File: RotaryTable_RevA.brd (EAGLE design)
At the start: 90 x 70 mm, 85 parts, among them CON1 USB_BMULTICOMP, CON2 ICSP, CON4 CON_5X2, CON5 CON_5X100MIL, CON6 CON_4X200MIL, IC1 PIC18F26J50SO28, IC2 LD1117, IC3 24AA16, IC4 74AHCT125, IC5 74HC14D, IC6 LMT86, IC7 ULN2003, IC8 MCP16311, SW1 PEC11R, SW2 PEC11R, SW3 PEC09, SW4 PEC09, X1 ABM3-8.000MHZ-D2Y-T, X2 BUZZER

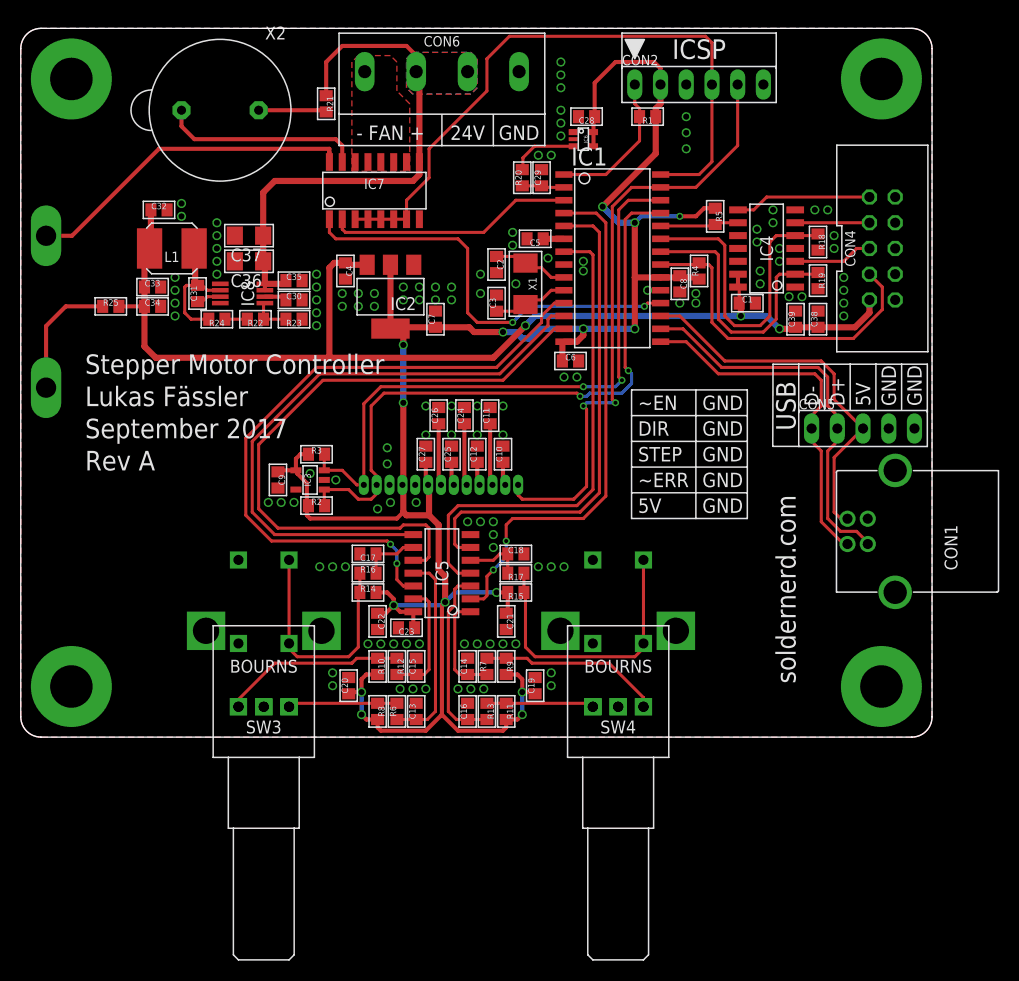
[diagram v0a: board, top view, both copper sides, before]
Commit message: USB header changed, header for external temperature sensor added, some ground vias added
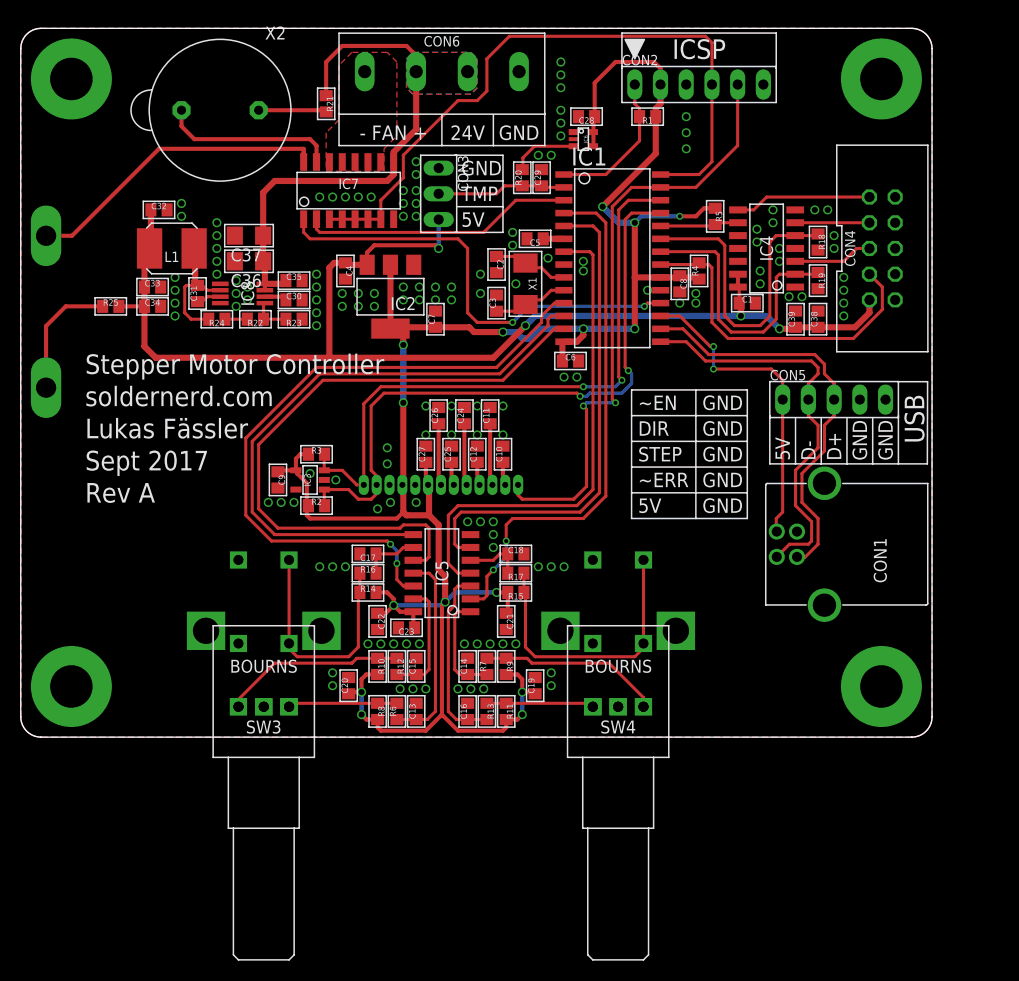
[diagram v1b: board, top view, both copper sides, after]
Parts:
- added CON3: CON_3X100MIL, 00Connector:100MIL_3X
- moved CON1 7.10 mm to (79.4, 19.1)
- moved CON5 4.04 mm to (80.3, 33.3)
- moved IC7 2.54 mm to (32.4, 54.0)
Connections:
- net +5V: now also CON3.3
- net GND: now also CON3.1
- net TEMP_SENSE: now also CON3.2
- net USB+: now also CON5.3; no longer CON5.2
- net USB-: now also CON5.2; no longer CON5.1
- net USB_SENSE: now also CON5.1; no longer CON5.3
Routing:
- net +5V: track 110.0 -> 121.5 mm, vias 3 -> 4
- net TEMP_SENSE: track 4.17 -> 12.8 mm
- net USB_SENSE: track 37.1 -> 31.2 mm, vias 0 -> 2
- net USB-: track 35.7 -> 40.2 mm
- net BUZZER: track 24.3 -> 26.9 mm
- net BUZZER_GND: track 19.9 -> 17.3 mm
- net BACKLIGHT_GND: track 33.8 -> 31.3 mm
- net BACKLIGHT: track 42.2 -> 44.8 mm
- net PGD/FAN: track 65.0 -> 67.1 mm
- net USB+: track 38.3 -> 40.4 mm
- net +24V: track 50.9 -> 49.9 mm
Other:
- board text added: "Sept 2017"
- board text added: "TMP"
- board text removed: "September 2017"

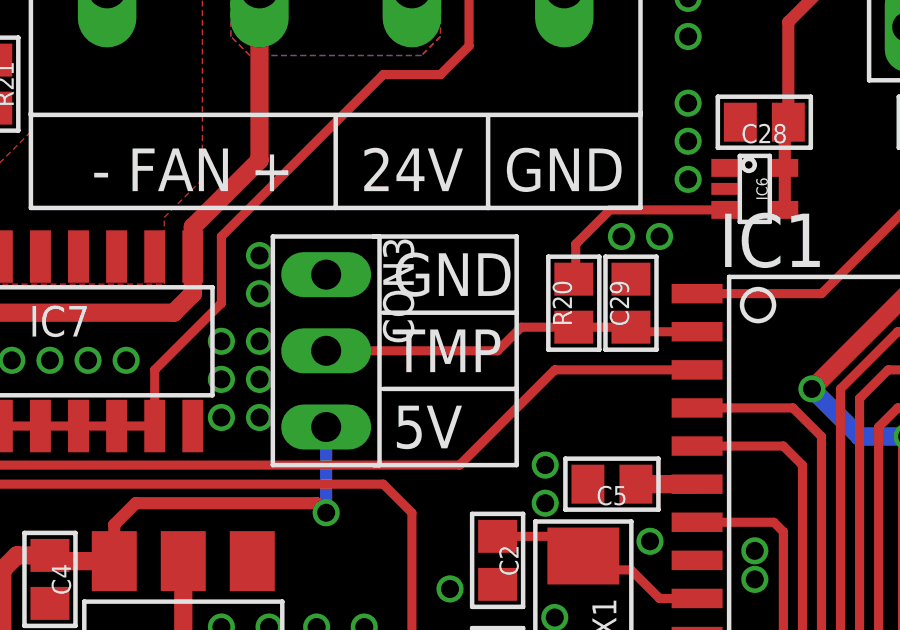
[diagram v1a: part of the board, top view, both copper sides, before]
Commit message: Bug related to external temperature sensing fixed
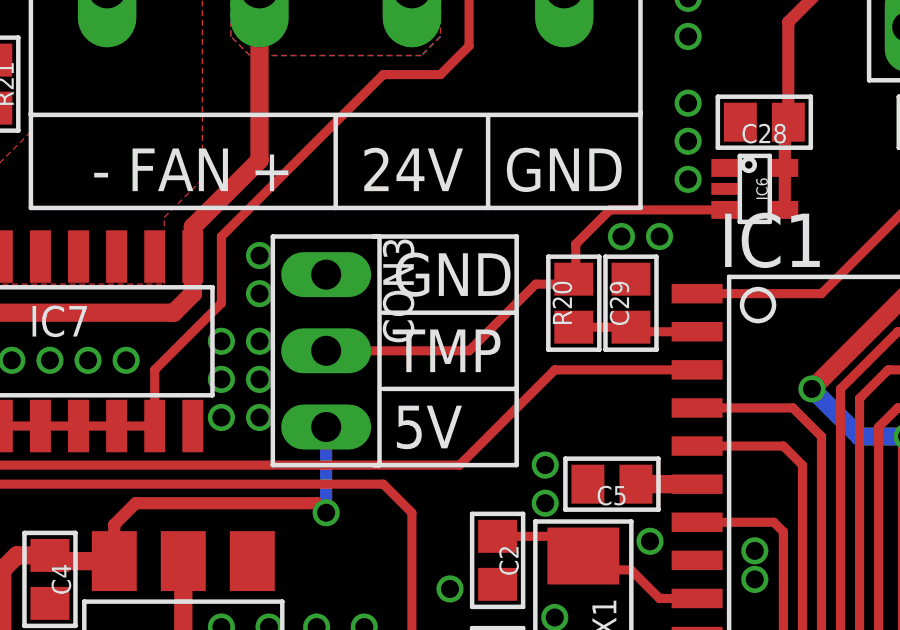
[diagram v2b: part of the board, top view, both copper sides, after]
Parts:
- L1: value (none) -> 22u
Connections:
- removed net N$2: IC6.3, R20.2
- new net TEMP: CON3.2, IC6.3, R20.2
- net TEMP_SENSE: no longer CON3.2
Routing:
- net TEMP: track 0.00 -> 15.9 mm
- net TEMP_SENSE: track 12.8 -> 4.17 mm
- net N$2: track 6.64 -> 0.00 mm
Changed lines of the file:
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@@
 <element name="C36" library="00Capacitor" package="C1206" value="10u 25V" x="22.5425" y="46.99" rot="R180"/>
 <element name="C37" library="00Capacitor" package="C1206" value="10u 25V" x="22.5425" y="49.53" rot="R180"/>
-<element name="L1" library="00Inductor" package="SRN5040" value="" x="14.9225" y="48.26" rot="R180"/>
+<element name="L1" library="00Inductor" package="SRN5040" value="22u" x="14.9225" y="48.26" rot="R180"/>
 <element name="R22" library="00Resistor" package="R0805" value="51k" x="23.1775" y="41.275" rot="R180"/>
 <element name="R23" library="00Resistor" package="R0805" value="10k" x="26.9875" y="41.275" rot="R180"/>
@@
 <wire x1="15.875" y1="60.325" x2="15.875" y2="61.9125" width="0.4064" layer="1"/>
 </signal>
-<signal name="N$2">
+<signal name="TEMP">
 <contactref element="IC6" pad="3"/>
 <contactref element="R20" pad="2"/>
@@
 <wire x1="49.595" y1="57.215" x2="50.735" y2="58.355" width="0.3048" layer="1"/>
 <wire x1="50.735" y1="58.355" x2="54.5625" y2="58.355" width="0.3048" layer="1"/>
+<contactref element="CON3" pad="2"/>
+<wire x1="41.275" y1="53.6575" x2="46.0375" y2="53.6575" width="0.3048" layer="1"/>
+<wire x1="46.0375" y1="53.6575" x2="48.26" y2="55.88" width="0.3048" layer="1"/>
+<wire x1="48.26" y1="55.88" x2="49.365" y2="55.88" width="0.3048" layer="1"/>
+<wire x1="49.365" y1="55.88" x2="49.53" y2="56.045" width="0.3048" layer="1"/>
 </signal>
 <signal name="TEMP_SENSE">
@@
 <wire x1="51.5875" y1="54.2925" x2="51.435" y2="54.445" width="0.3048" layer="1"/>
 <wire x1="51.435" y1="54.445" x2="49.53" y2="54.445" width="0.3048" layer="1"/>
-<contactref element="CON3" pad="2"/>
-<wire x1="41.275" y1="53.6575" x2="46.99" y2="53.6575" width="0.3048" layer="1"/>
-<wire x1="49.53" y1="54.445" x2="47.7775" y2="54.445" width="0.3048" layer="1"/>
-<wire x1="47.7775" y1="54.445" x2="46.99" y2="53.6575" width="0.3048" layer="1"/>
 </signal>
 <signal name="N$4">

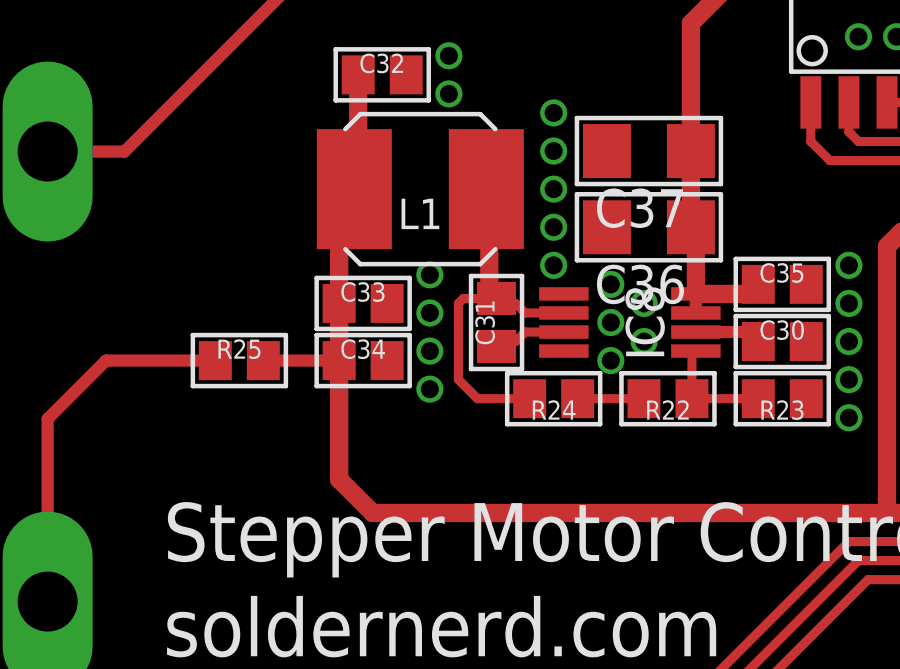
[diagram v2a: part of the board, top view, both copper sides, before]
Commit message: Error in schematic and in board layout fixed. Voltage regulator feedback was taken from the wrong side of the coil.
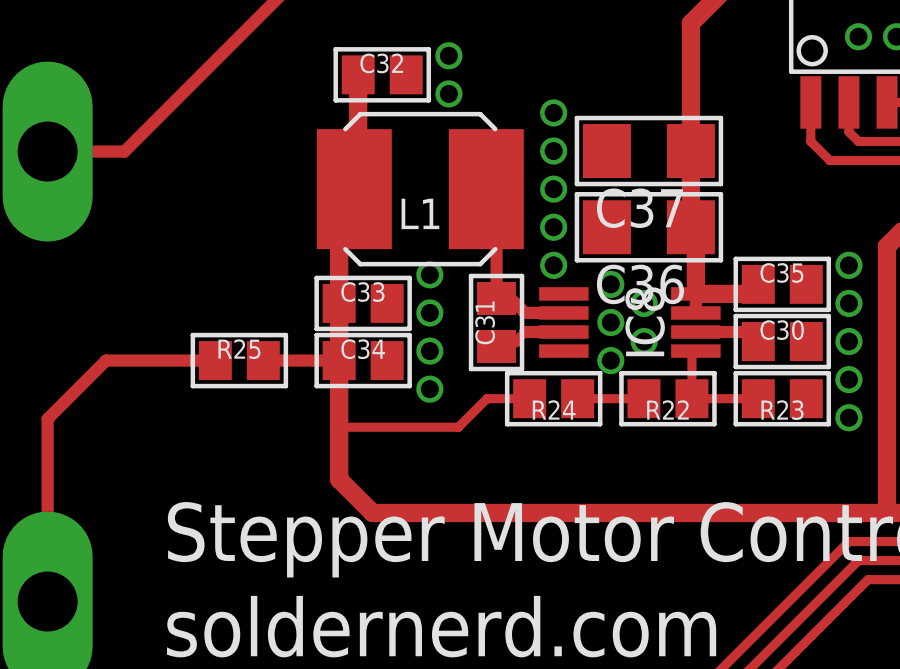
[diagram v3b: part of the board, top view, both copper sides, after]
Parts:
- IC7: value ULN2003 -> TPL7407
- IC8: value MCP16311 -> MCP16312
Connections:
- removed net N$16: C31.2, IC8.6, L1.1, R24.2
- new net N$2: C31.2, IC8.6, L1.1
- net +5V: now also R24.2
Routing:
- net N$16: track 12.7 -> 0.00 mm
- net +5V: track 121.5 -> 128.3 mm
- net N$2: track 0.00 -> 6.43 mm
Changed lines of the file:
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@@
 <element name="C4" library="00Capacitor" package="C0805" value="10u" x="32.0675" y="46.0375" rot="R270"/>
 <element name="C7" library="00Capacitor" package="C0805" value="10u" x="40.9575" y="41.275" rot="R90"/>
-<element name="IC7" library="00Transistor" package="SO16" value="ULN2003" x="32.385" y="53.975"/>
+<element name="IC7" library="00Transistor" package="SO16" value="TPL7407" x="32.385" y="53.975"/>
 <element name="IC6" library="00Sensor" package="SC70-5" value="LMT86" x="55.5625" y="59.055" rot="R270"/>
 <element name="C28" library="00Capacitor" package="C0805" value="100n" x="55.88" y="61.2775" rot="R180"/>
@@
 <element name="X2" library="00MyParts" package="BUZZER_14MM" value="BUZZER" x="19.685" y="61.9125"/>
 <element name="R21" library="00Resistor" package="R0805" value="10k" x="30.1625" y="62.5475" rot="R270"/>
-<element name="IC8" library="00VoltageRegulator" package="MSOP8" value="MCP16311" x="21.9075" y="43.815" rot="R180"/>
+<element name="IC8" library="00VoltageRegulator" package="MSOP8" value="MCP16312" x="21.9075" y="43.815" rot="R180"/>
 <element name="C30" library="00Capacitor" package="C0805" value="1u" x="26.9875" y="43.18"/>
 <element name="C31" library="00Capacitor" package="C0805" value="100n" x="17.4625" y="43.815" rot="R90"/>
@@
 <wire x1="30.48" y1="37.465" x2="13.335" y2="37.465" width="0.6096" layer="1"/>
 <wire x1="13.335" y1="37.465" x2="12.2175" y2="38.5825" width="0.6096" layer="1"/>
-<wire x1="12.2175" y1="38.5825" x2="12.2175" y2="42.545" width="0.6096" layer="1"/>
+<wire x1="12.2175" y1="38.5825" x2="12.2175" y2="40.3225" width="0.6096" layer="1"/>
+<wire x1="12.2175" y1="40.3225" x2="12.2175" y2="42.545" width="0.6096" layer="1"/>
 <wire x1="30.48" y1="37.465" x2="46.6725" y2="37.465" width="0.6096" layer="1"/>
 <wire x1="46.6725" y1="37.465" x2="49.8475" y2="40.64" width="0.6096" layer="1"/>
@@
 <via x="41.275" y="48.26" extent="1-16" drill="0.6"/>
 <wire x1="41.275" y1="51.1175" x2="41.275" y2="48.26" width="0.4064" layer="16"/>
+<contactref element="R24" pad="2"/>
+<wire x1="18.5675" y1="41.275" x2="17.145" y2="41.275" width="0.3048" layer="1"/>
+<wire x1="17.145" y1="41.275" x2="16.1925" y2="40.3225" width="0.3048" layer="1"/>
+<wire x1="16.1925" y1="40.3225" x2="12.2175" y2="40.3225" width="0.3048" layer="1"/>
 </signal>
 <signal name="N$3">
@@
 <contactref element="IC8" pad="7"/>
 <contactref element="C31" pad="1"/>
-<wire x1="19.7075" y1="43.4975" x2="18.415" y2="43.4975" width="0.3048" layer="1"/>
+<wire x1="19.7075" y1="43.4975" x2="18.415" y2="43.4975" width="0.4064" layer="1"/>
 <wire x1="18.415" y1="43.4975" x2="18.0975" y2="43.18" width="0.3048" layer="1"/>
-<wire x1="18.0975" y1="43.18" x2="17.6275" y2="43.18" width="0.3048" layer="1"/>
+<wire x1="18.0975" y1="43.18" x2="17.6275" y2="43.18" width="0.4064" layer="1"/>
 <wire x1="17.6275" y1="43.18" x2="17.4625" y2="43.015" width="0.3048" layer="1"/>
 </signal>
@@
 <wire x1="23.9775" y1="42.8625" x2="23.9775" y2="41.275" width="0.3048" layer="1"/>
 </signal>
-<signal name="N$16">
-<contactref element="IC8" pad="6"/>
-<contactref element="C31" pad="2"/>
-<contactref element="L1" pad="1"/>
-<contactref element="R24" pad="2"/>
-<wire x1="19.7075" y1="44.1325" x2="18.415" y2="44.1325" width="0.3048" layer="1"/>
-<wire x1="18.415" y1="44.1325" x2="18.0975" y2="44.45" width="0.3048" layer="1"/>
-<wire x1="18.0975" y1="44.45" x2="17.6275" y2="44.45" width="0.3048" layer="1"/>
-<wire x1="17.6275" y1="44.45" x2="17.4625" y2="44.615" width="0.3048" layer="1"/>
-<wire x1="17.4625" y1="44.615" x2="16.3575" y2="44.615" width="0.3048" layer="1"/>
-<wire x1="16.3575" y1="44.615" x2="16.1925" y2="44.45" width="0.3048" layer="1"/>
-<wire x1="16.1925" y1="44.45" x2="16.1925" y2="41.91" width="0.3048" layer="1"/>
-<wire x1="16.1925" y1="41.91" x2="16.8275" y2="41.275" width="0.3048" layer="1"/>
-<wire x1="16.8275" y1="41.275" x2="18.5675" y2="41.275" width="0.3048" layer="1"/>
-<wire x1="17.2225" y1="44.855" x2="17.4625" y2="44.615" width="0.6096" layer="1"/>
-<wire x1="17.2225" y1="44.855" x2="17.2225" y2="48.16" width="0.6096" layer="1"/>
-<wire x1="17.2225" y1="48.16" x2="17.1225" y2="48.26" width="0.6096" layer="1"/>
-</signal>
 <signal name="N$11">
 <contactref element="R22" pad="2"/>
@@
 <wire x1="4.445" y1="42.545" x2="8.09" y2="42.545" width="0.4064" layer="1"/>
 </signal>
+<signal name="N$2">
+<contactref element="IC8" pad="6"/>
+<contactref element="L1" pad="1"/>
+<contactref element="C31" pad="2"/>
+<wire x1="19.7075" y1="44.1325" x2="18.415" y2="44.1325" width="0.4064" layer="1"/>
+<wire x1="18.415" y1="44.1325" x2="17.9325" y2="44.615" width="0.4064" layer="1"/>
+<wire x1="17.9325" y1="44.615" x2="17.4625" y2="44.615" width="0.3048" layer="1"/>
+<wire x1="17.4625" y1="44.615" x2="17.4625" y2="48.26" width="0.4064" layer="1"/>
+<wire x1="17.4625" y1="48.26" x2="17.1225" y2="48.26" width="0.4064" layer="1"/>
+</signal>
 </signals>
